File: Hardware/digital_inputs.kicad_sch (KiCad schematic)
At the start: 0 parts

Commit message: scheme update
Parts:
- added C23: 100n, symbol Device:C_Small
- added D23, D8: SP0504BAJT, Package_TO_SOT_SMD:SOT-353_SC-70-5, symbol Power_Protection:SP0504BAJT
- added D6: LD_DI0, symbol Device:LED_Small
- added R10: 3k3, symbol Device:R_Small
- added R11, R9: 10k, symbol Device:R_Small
- added R8: 4k7, symbol Device:R_Small
- added U3: TCMT1100, Package_SO:SOP-4_4.4x2.6mm_P1.27mm, symbol Isolator:TCMT1100
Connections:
- new net: C23.1, R9.2, U3.1
- new net: R10.2, U3.2
- new net: R11.1, R8.2, U3.4
- new net: D6.2 (A), R10.1
- new net +3V3: R8.1
- new net 24V IN: R9.1
- new net GND: C23.2, D6.1 (K), U3.3
- new net MCU GPIO OUT: R11.2
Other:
- title: (none) -> PLC ON STM

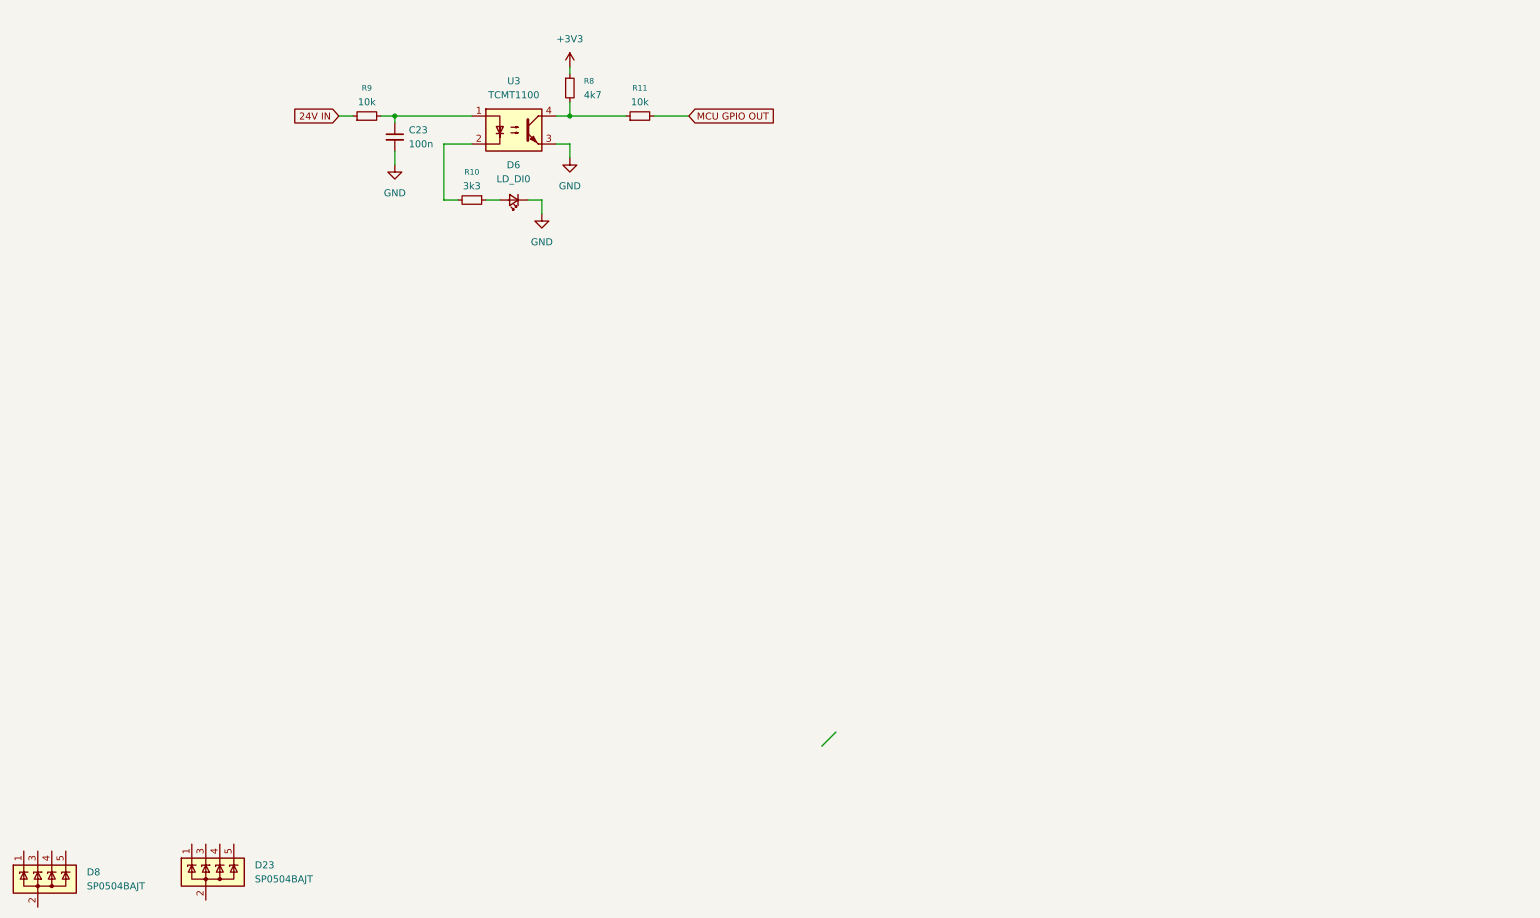
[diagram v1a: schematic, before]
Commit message: schematic update
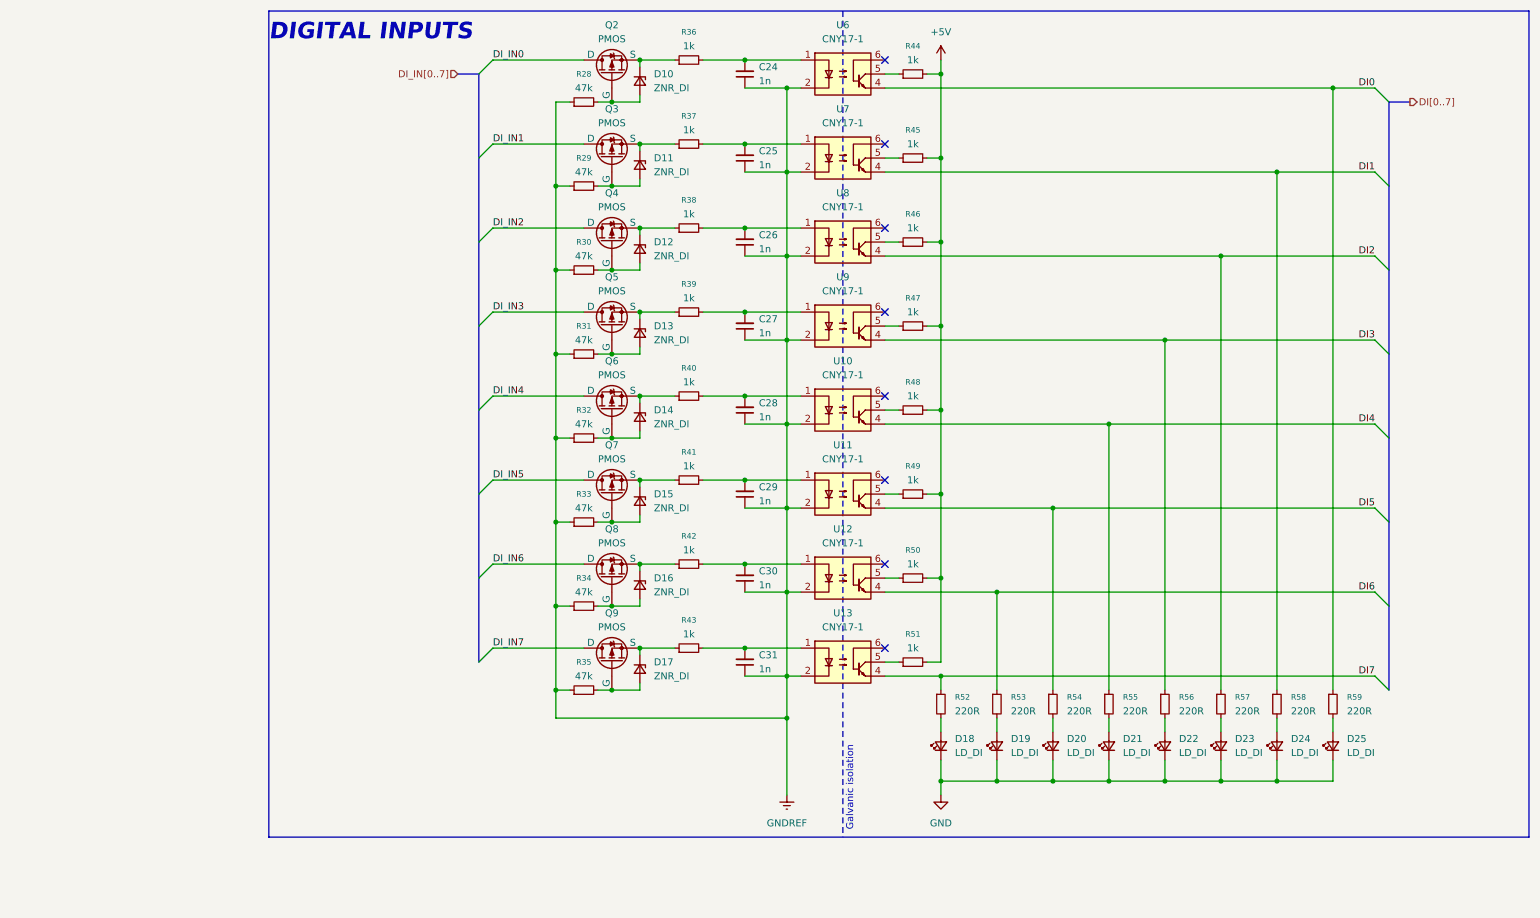
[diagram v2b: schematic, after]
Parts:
- removed C23: 100n, symbol Device:C_Small
- removed D23, D8: SP0504BAJT, Package_TO_SOT_SMD:SOT-353_SC-70-5, symbol Power_Protection:SP0504BAJT
- removed D6: LD_DI0, symbol Device:LED_Small
- removed R10: 3k3, symbol Device:R_Small
- removed R11, R9: 10k, symbol Device:R_Small
- removed R8: 4k7, symbol Device:R_Small
- removed U3: TCMT1100, Package_SO:SOP-4_4.4x2.6mm_P1.27mm, symbol Isolator:TCMT1100
- added C24, C25, C26, C27, C28, C29, C30, C31: 1n, symbol Device:C_Small
- added D10, D11, D12, D13, D14, D15, D16, D17: ZNR_DI, symbol Device:D_Zener_Small
- added D18, D19, D20, D21, D22, D23, D24, D25: LD_DI, symbol Device:LED_Small
- added Q2, Q3, Q4, Q5, Q6, Q7, Q8, Q9: PMOS, symbol Simulation_SPICE:PMOS
- added R28, R29, R30, R31, R32, R33, R34, R35: 47k, symbol Device:R_Small
- added R36, R37, R38, R39, R40, R41, R42, R43, R44, R45, R46, R47, R48, R49, R50, R51: 1k, symbol Device:R_Small
- added R52, R53, R54, R55, R56, R57, R58, R59: 220R, symbol Device:R_Small
- added U10, U11, U12, U13, U6, U7, U8, U9: CNY17-1, symbol Isolator:CNY17-1
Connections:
- net GND: now also D18.1 (K), D19.1 (K), D20.1 (K), D21.1 (K), D22.1 (K), D23.1 (K), D24.1 (K), D25.1 (K)
- new net: C27.2, R39.2, U9.1
- new net: D14.2 (A), Q6.2 (G), R32.2
- new net: C28.2, R40.2, U10.1
- new net: D17.1 (K), Q9.3 (S), R43.1
- new net: C31.2, R43.2, U13.1
- new net: D15.2 (A), Q7.2 (G), R33.2
- new net: C26.2, R38.2, U8.1
- new net: D16.1 (K), Q8.3 (S), R42.1
- new net: C30.2, R42.2, U12.1
- new net: R46.1, U8.5
- new net: D21.2 (A), R55.2
- new net: D24.2 (A), R58.2
- new net: D16.2 (A), Q8.2 (G), R34.2
- new net: R48.1, U10.5
- new net: D10.2 (A), Q2.2 (G), R28.2
- new net: D25.2 (A), R59.2
- new net: D10.1 (K), Q2.3 (S), R36.1
- new net: C29.2, R41.2, U11.1
- new net: R49.1, U11.5
- new net: D12.2 (A), Q4.2 (G), R30.2
- new net: D17.2 (A), Q9.2 (G), R35.2
- new net: R47.1, U9.5
- new net: D13.1 (K), Q5.3 (S), R39.1
- new net: D13.2 (A), Q5.2 (G), R31.2
- new net: D11.2 (A), Q3.2 (G), R29.2
- new net: D11.1 (K), Q3.3 (S), R37.1
- new net: R44.1, U6.5
- new net: D22.2 (A), R56.2
- new net: D12.1 (K), Q4.3 (S), R38.1
- new net: R50.1, U12.5
- new net: C25.2, R37.2, U7.1
- new net: R51.1, U13.5
- new net: D18.2 (A), R52.2
- new net: D14.1 (K), Q6.3 (S), R40.1
- new net: C24.2, R36.2, U6.1
- new net: R45.1, U7.5
- new net: D20.2 (A), R54.2
- new net: D15.1 (K), Q7.3 (S), R41.1
- new net: D19.2 (A), R53.2
- new net: D23.2 (A), R57.2
- new net +5V: R44.2, R45.2, R46.2, R47.2, R48.2, R49.2, R50.2, R51.2
- new net DI0: R59.1, U6.4
- new net DI1: R58.1, U7.4
- new net DI2: R57.1, U8.4
- new net DI3: R56.1, U9.4
- new net DI4: R55.1, U10.4
- new net DI5: R54.1, U11.4
- new net DI6: R53.1, U12.4
- new net DI7: R52.1, U13.4
- new net DI_IN0: Q2.1 (D)
- new net DI_IN1: Q3.1 (D)
- new net DI_IN2: Q4.1 (D)
- new net DI_IN3: Q5.1 (D)
- new net DI_IN4: Q6.1 (D)
- new net DI_IN5: Q7.1 (D)
- new net DI_IN6: Q8.1 (D)
- new net DI_IN7: Q9.1 (D)
- new net GNDREF: C24.1, C25.1, C26.1, C27.1, C28.1, C29.1, C30.1, C31.1, R28.1, R29.1, R30.1, R31.1, R32.1, R33.1, R34.1, R35.1, U10.2, U11.2, U12.2, U13.2, U6.2, U7.2, U8.2, U9.2
- no-connect marks 0 -> 8
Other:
- note added: "DIGITAL INPUTS"
- note added: "Galvanic isolation"
